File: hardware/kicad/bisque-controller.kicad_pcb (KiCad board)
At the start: 4 copper layers, 100 x 100 mm, 144 parts, among them J1 USB-C, J10 AUX, J11 INPUTS, J12 CT, J13 AC_SENSE_DNP, J14 QWIIC, J2 5V_IN, J3 TC1_K, J4 SSR1, J5 DISPLAY, J6 NAV_SW, J7 AUX, J8 TC2_K, J9 SSR2, Q2 AO3400A, Q3 AO3400A, Q4 AO3401A, Q5 AO3400A, Q6 AO3400A, SW1 RESET, SW2 BOOT, U1 ESP32-S3-WROOM-1U-N16R2, U2 AMS1117-3.3, U3 MAX31856MUD+, U4 USBLC6-2SC6, U5 MAX31856MUD+, U6 ULN2003A, U7 ADE7953ACPZ, Y1 3.579545MHz

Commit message: feat(hw): three parts off the feeder bill, $27 -> $18
JLCPCB charges $3 per unique Extended part to mount a feeder on Economic
PCBA. This board owed it on nine. Six of those are structural and stay:
the fee-free library contains *no connectors at all*, so J1 and J14 cannot
be avoided at any price, and the module, both MAX31856s, the ADE7953 and
its 3.579545 MHz crystal have no fee-free equivalent either. $18 is the
floor short of hand-soldering J14.

The other three had substitutes that are better parts on their own terms:

  * U4, D5 and D6 collapse onto ONE Preferred SRV05-4 (C7420376),
    replacing an Extended SRV05-4 line (C558418) and a USBLC6-2SC6
    (C7519). Worth $6. Read off the two datasheets rather than assumed:
    it takes U4 from IEC 61000-4-2 level 4 and no more (+-8 kV contact,
    +-15 kV air) to +-30 kV on both, and from 3.5 pF max line capacitance
    to 1.0 pF - better on the one pair whose impedance this board cares
    about.
  * R31/R34 move from 6.8 to 5.1 ohm (C17724, Basic). Worth $3. JLCPCB
    stocks no 6.8 ohm resistor in either fee-free library in ANY package,
    so one value was renting a feeder. It costs range, not accuracy: 100 A
    now reads 361 mV, 72% of the ADE7953's full scale instead of 96%, and
    full scale moves out to ~139 A rms. This also retires the C17774
    sourcing flag - that line was down to ~970 units.

Two more were never chargeable and the tooling said they were. LCSC's
third tuple field was documented as basic_part and read as "is Basic",
but *two* libraries are fee-free on Economic: Basic (351 parts) and
Preferred Extended (1235), the latter being parts JLCPCB keeps mounted
but has moved out of Basic. C107114 (30 pF) and C7420333 (BAT54S) are
Preferred, so gen_jlc printed $33 for a board that owed $27. The field is
now fee_free and carries the API predicate it actually means. The
distinction does not appear on the part page's category line, only in
componentLibraryType/preferredComponentFlag, which is why 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
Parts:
- R31, R34: value 6R8 -> 5R1
- U4: value USBLC6-2SC6 -> SRV05-4
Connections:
- U4 pad 1: USB_DN -> (no net)
- U4 pad 3: USB_DP -> (no net)
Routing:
- net WDT_KICK: track 68.6 -> 35.2 mm, vias 4 -> 2
- net USB_DP: track 40.1 -> 39.1 mm, vias 6 -> 7

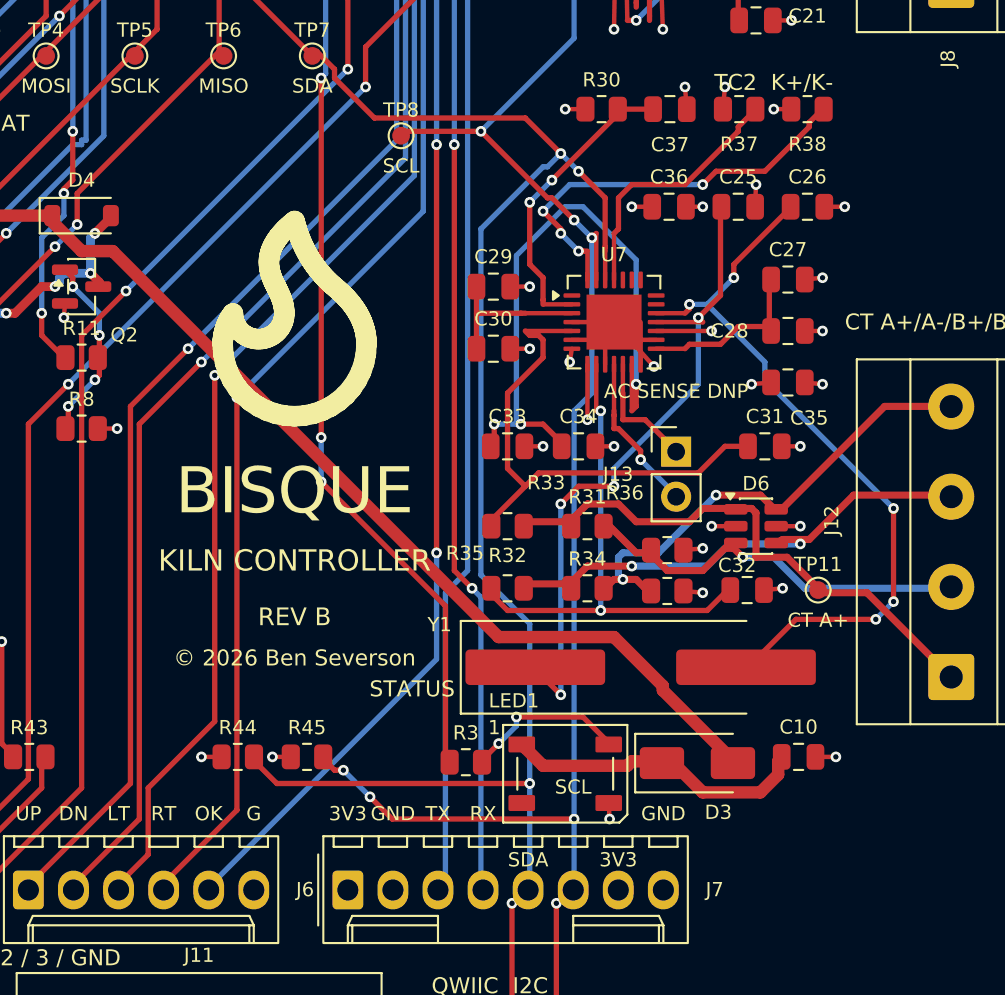
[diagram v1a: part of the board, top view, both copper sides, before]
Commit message: feat(hw): replace the crystal with an oscillator, and the loop with a wire
Y1 was a 3.579545 MHz crystal 19.5 mm from U7 with its two load caps 26 mm
the far side of the IC: ADE_CLKIN 37.5 mm and ADE_CLKOUT 41.6 mm, nine vias
between them, two high-impedance resonant nodes strung across the busiest
corner of the board. It is now a packaged oscillator. ADE_CLKIN is 10.53 mm
of driven CMOS and ADE_CLKOUT does not exist.

The swap inverts the usual default and it is worth saying why. A crystal is
normally right: a tenth the cost, microamps against 5 mA, and the IC's own
inverter is characterised for one. None of that applies here - $0.23 on a
$19 BOM, 5 mA beside the ESP32's 240 mA on a mains-fed rail, and ±50 ppm is
100x better than an IRMS reading needs. Meanwhile the one thing a crystal
demands is the one thing this corner cannot give. 3.579545 MHz is low, so
the quartz blank is large and every 2-terminal part at this frequency is
HC-49S: 19.75 mm of pad on the hand-solder land we were using, 13.00 mm even
on the standard one. U7's ring is entirely VINTA/VINTD/VDD/REF decoupling
that ADE7953 Rev C p.67 says must stay closest to the chip, so nothing that
size fits beside it and no re-placement was ever going to work.

Everything the datasheet needed to answer, it answers. Pin 1 is left OPEN on
the Measurement Circuit's own switch table - H and OPEN both give
"Oscillation out", only L is High Z - so no pull-up. The pinout is confirmed
twice, by that pin table and by LCSC's symbol: 1 Tri-state / 2 GND / 3 OUT /
4 Vdd, which is also what KiCad's Oscillator:ASE-xxxMHz carries. V_OH >= 90%
Vdd = 2.97 V against the ADE7953's 2.4 V V_INH, and the 15 pF max output
load dwarfs CLKIN plus 10 mm of track. Datasheet saved alongside; I had
earlier called it unpublished, which was a fetch failure (datasheet.lcsc.com
needs a referer) misread as absence.

Placed 7.8 mm from CLKIN, not the 2.5 mm it fits at. U7 is in FANOUT, so
pre-seeded escape stubs and plane vias own a ring reachi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
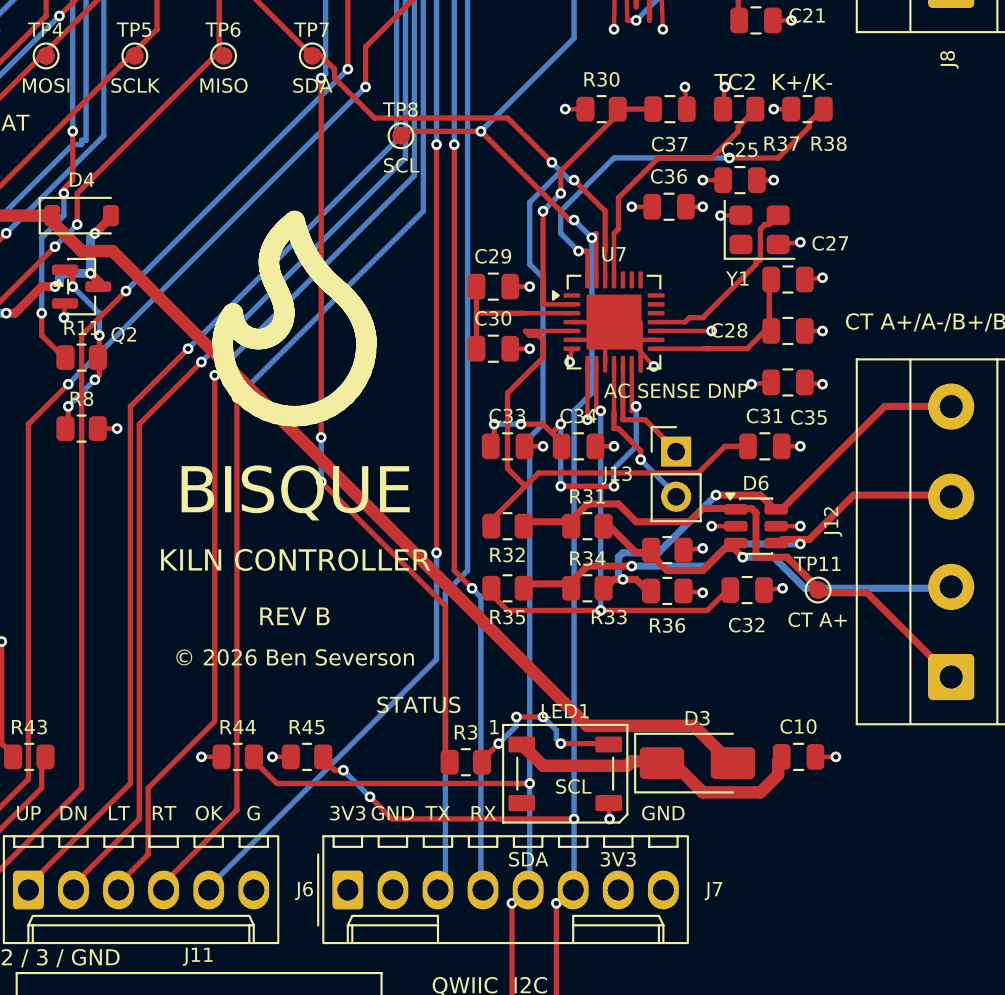
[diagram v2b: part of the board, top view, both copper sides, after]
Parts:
- removed C26: 30pF, C_0805_2012Metric
- C25: value 30pF -> 100nF
- Y1: value 3.579545MHz -> 3.579545MHz XO; footprint Crystal_SMD_HC49-SD_HandSoldering -> Oscillator_SMD_Abracon_ASE-4Pin_3.2x2.5mm
- moved Y1 25.5 mm to (103.2, 66.8)
- moved C25 1.50 mm to (102.1, 64.0)
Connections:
- C25 pad 1: ADE_CLKIN -> +3V3
- U7 pad 19: ADE_CLKOUT -> (no net)
- Y1 pad 1: ADE_CLKIN -> (no net)
- Y1 pad 2: ADE_CLKOUT -> GND
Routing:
- net ADE_CLKOUT: track 41.6 -> 0.00 mm, vias 5 -> 0
- net ADE_CLKIN: track 37.5 -> 10.5 mm, vias 4 -> 0
- net ADE_REF: track 35.6 -> 21.0 mm, vias 3 -> 6
- net I2C_SDA: track 123.1 -> 119.8 mm
- net +3V3: track 53.8 -> 56.1 mm, vias 38 -> 40
- net ADE_CS: track 23.5 -> 22.1 mm, vias 4 -> 2
- net ADE_RESET: track 17.1 -> 16.5 mm
- net WS_DIN: track 9.21 -> 9.45 mm, vias 2 -> 4

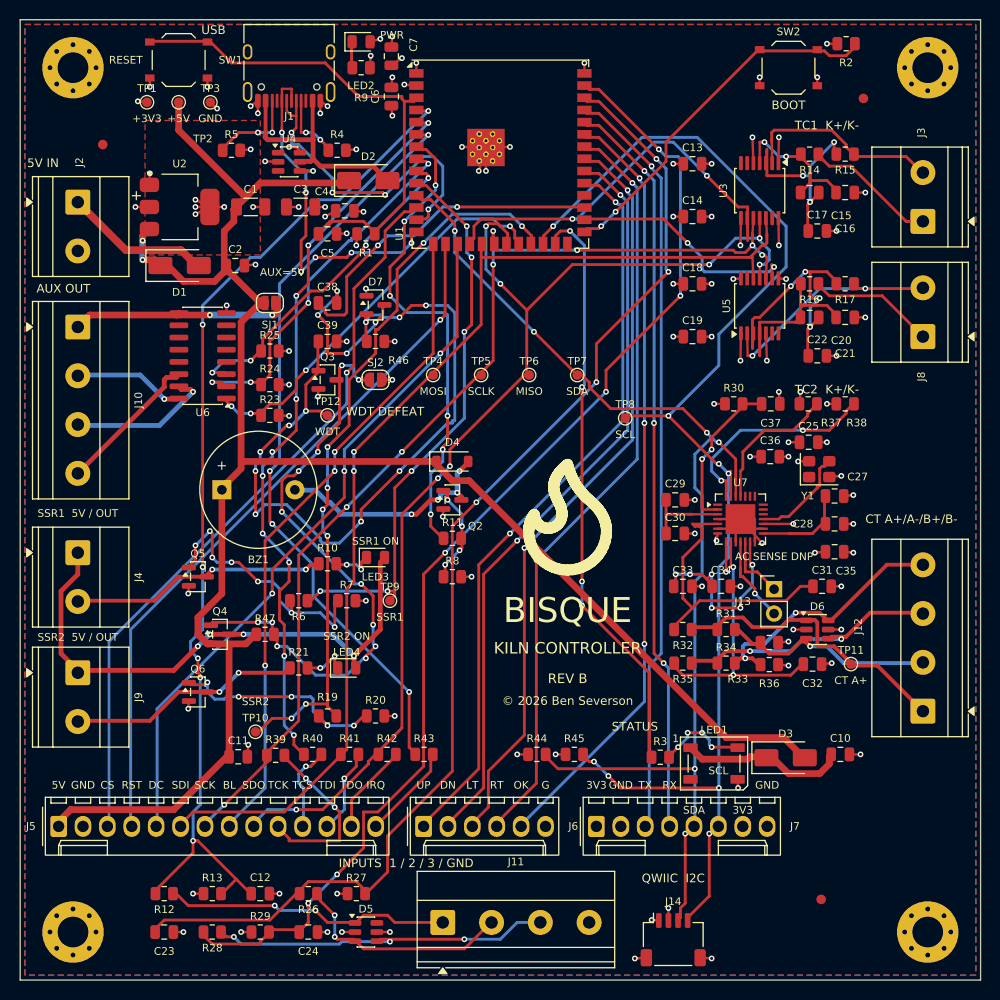
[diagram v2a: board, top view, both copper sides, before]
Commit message: feat(hw): a legend per terminal, and the parts moved to make room
Every screw terminal on this board stacks its screws VERTICALLY and every
legend beside them was a HORIZONTAL list -- `SSR1  5V / OUT`, `TC1  K+/K-`,
`CT A+/A-/B+/B-`. Reading left to right says nothing about which screw is
which; you had to find the pin-1 triangle and count. On the SSR and CT blocks
that is the difference between a legend and a hint.

`gen_pcb.PIN_LEGENDS` replaces them with 50 generated legends, one per pin,
printed beside that pin's own pad. Nothing in the table is a coordinate: pad
centres come from the real footprint and the standoff from the real drawn
body, so a connector that moves takes its legends with it. Each declares the
axis carrying its meaning -- x for a pin name over a pin, y for a mark beside
a screw -- and that is a hard constraint, not a weight: `silk.py` refuses any
candidate off it and `kicad_build.py` fails the build if one lands off it
anyway. `W_LATERAL` stays as the fallback guess, and it is backwards for
every vertical terminal, which is why declaring beats guessing.

Three ties in the placer had to be re-decided for that to hold:

  - a reference designator may not take a seated legend's space
  - nor may a legend yield to a designator merely SEEDED in it (board texts
    are scored before references are placed, so `K-` twice fled J3's lower
    screw for `R15`'s unplaced library-default position)
  - nor may a designator slot INTO a row: `J11` printed `IN1 IN2 J11 IN3 GND`
    for free, because the glyphs cleared by 0.80 mm and CLEAR_CROWD is 0.5

Parts moved where no legend could fit, which is the honest fix and was
`check_silk.ON_PART_OK`'s whole point. That list is now EMPTY:

  - LED1 + R3 + D3 + C10 out of J7's pin-name band. A 5 x 5 mm WS2812 is
    wider than three pin pitches and was sitting on the labels for pins 5-7,
    so the row printed `3V3 GND TX RX . . . GND` -- a 10 mm hole, on the one
    header carrying I2C and a 3.3 V rail.
  - SW1 besi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
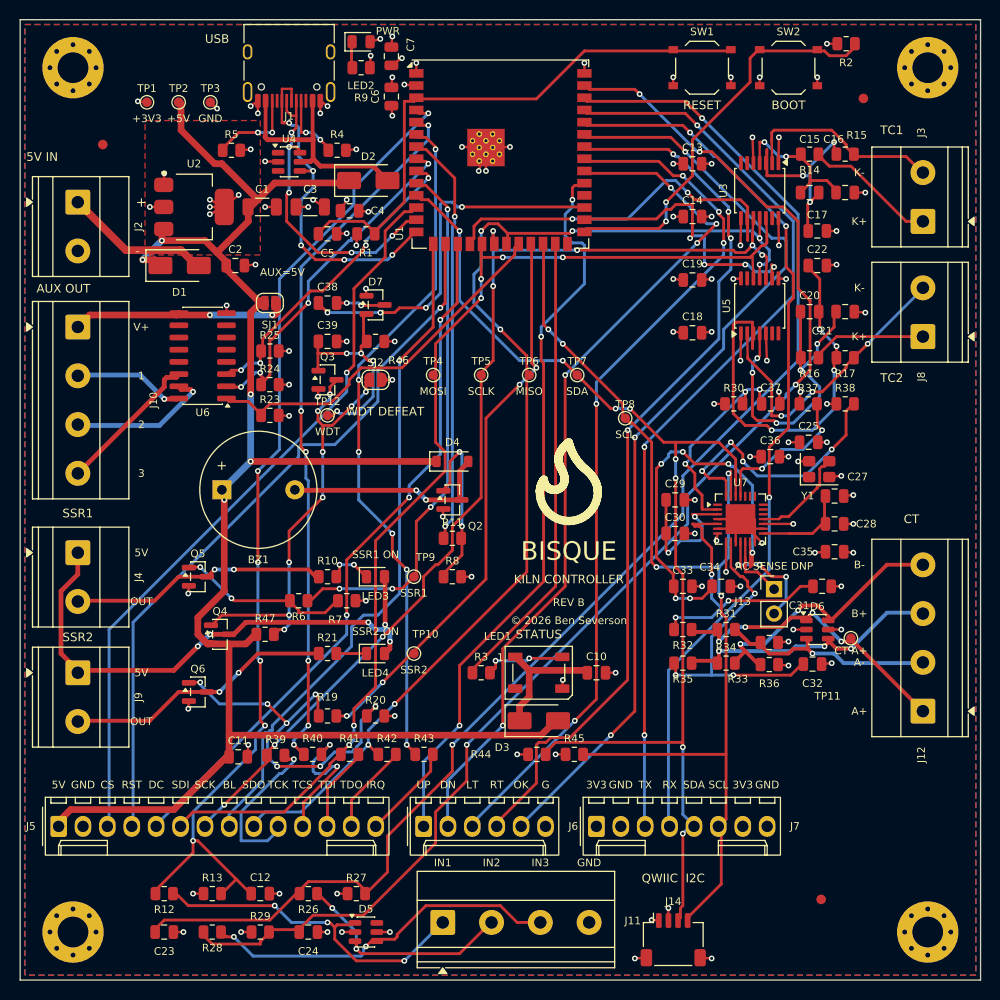
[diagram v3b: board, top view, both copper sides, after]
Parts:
- moved SW1 54.5 mm to (91.0, 25.0)
- moved C10 26.8 mm to (80.0, 88.0)
- moved D3 26.0 mm to (74.0, 93.0)
- moved R3 20.6 mm to (68.0, 88.0)
- moved LED1 20.6 mm to (74.0, 88.0)
- moved TP10 18.4 mm to (61.0, 86.0)
- moved C22 9.40 mm to (103.0, 45.6)
- moved R16 7.70 mm to (102.2, 55.2)
- moved R17 7.70 mm to (105.9, 55.2)
- moved C19 5.90 mm to (90.0, 47.1)
- moved C18 5.10 mm to (90.0, 52.6)
- moved TP9 3.54 mm to (61.0, 78.0)
- moved LED4 3.35 mm to (57.0, 86.0)
- moved R21 3.35 mm to (52.0, 86.0)
- moved TP11 2.70 mm to (106.5, 84.4)
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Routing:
- net WDT_HOLD: track 77.6 -> 23.4 mm, vias 10 -> 4
- net I2C_SCL: track 139.4 -> 112.8 mm, vias 8 -> 5
- net ADE_REF: track 21.0 -> 42.3 mm
- net SSR2_CTRL: track 77.2 -> 59.1 mm, vias 8 -> 4
- net +5V: track 201.7 -> 183.9 mm, vias 2 -> 5
- net SSR_PG: track 63.6 -> 45.8 mm, vias 12 -> 9
- net BTN_SEL: track 80.6 -> 98.0 mm
- net TC2_N_F: track 27.6 -> 44.3 mm
- net TXD0: track 79.3 -> 95.9 mm, vias 1 -> 3
- net IN3: track 123.1 -> 139.7 mm, vias 6 -> 4
- net TC2_P_F: track 18.2 -> 34.7 mm, vias 0 -> 5
- net SSR2_GATE: track 23.9 -> 40.4 mm, vias 5 -> 7
- net IN2: track 125.5 -> 141.9 mm, vias 4 -> 2
- net RXD0: track 77.6 -> 93.7 mm
- net BTN_RIGHT: track 79.9 -> 94.0 mm, vias 2 -> 4
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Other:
- board text added: "1"
- board text added: "2"
- board text added: "3"
- board text added: "A+"
- board text added: "A-"
- board text added: "B+"
- board text added: "B-"
- board text added: "CT"
- board text added: "IN1"
- board text added: "IN2"
- board text added: "IN3"
- board text added: "K+"
- board text added: "K-"
- board text added: "OUT"
- board text added: "TC1"
- board text added: "TC2"
- board text added: "V+"
- board text removed: "CT A+/A-/B+/B-"
- board text removed: "INPUTS 1 / 2 / 3 / GND"
- board text removed: "SSR1 5V / OUT"
- board text removed: "SSR2 5V / OUT"
- board text removed: "TC1 K+/K-"
- board text removed: "TC2 K+/K-"
